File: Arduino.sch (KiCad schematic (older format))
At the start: 9 parts

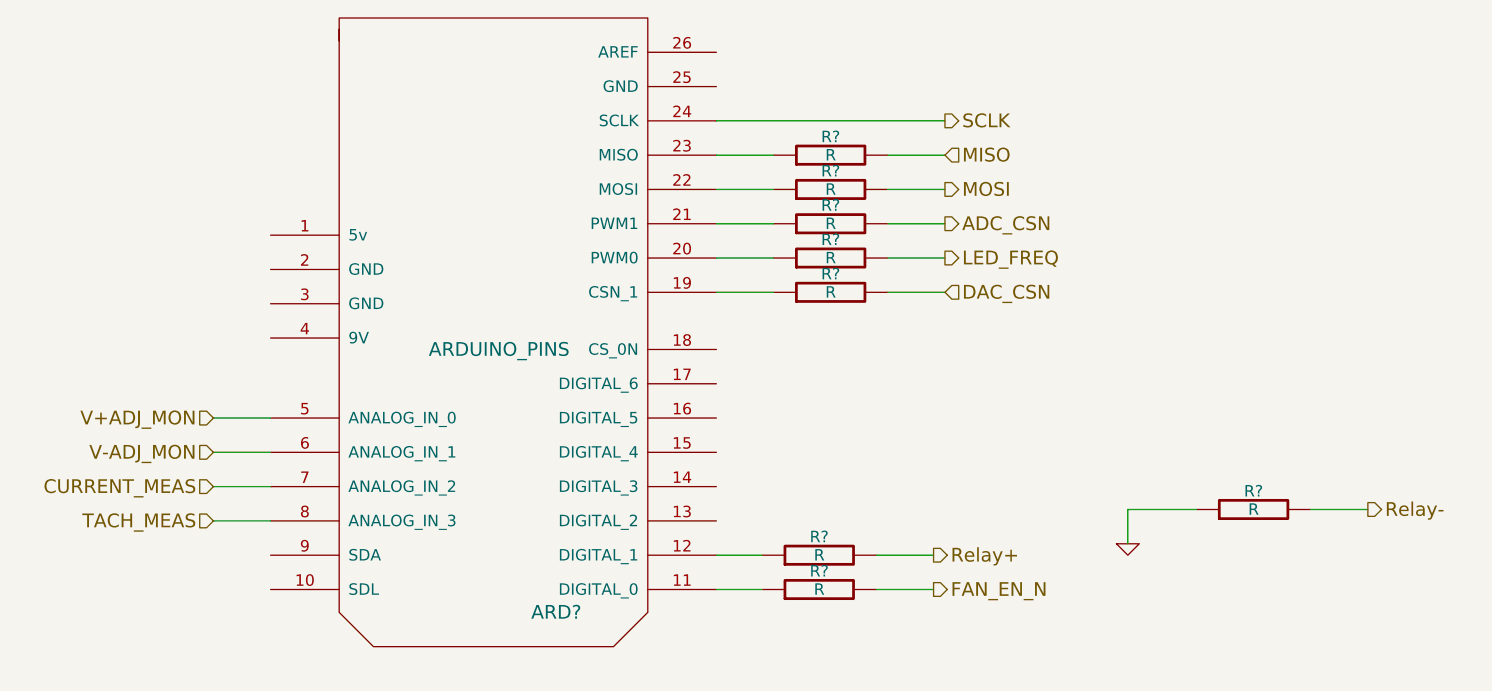
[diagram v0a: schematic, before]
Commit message: Fan/Current mode redo
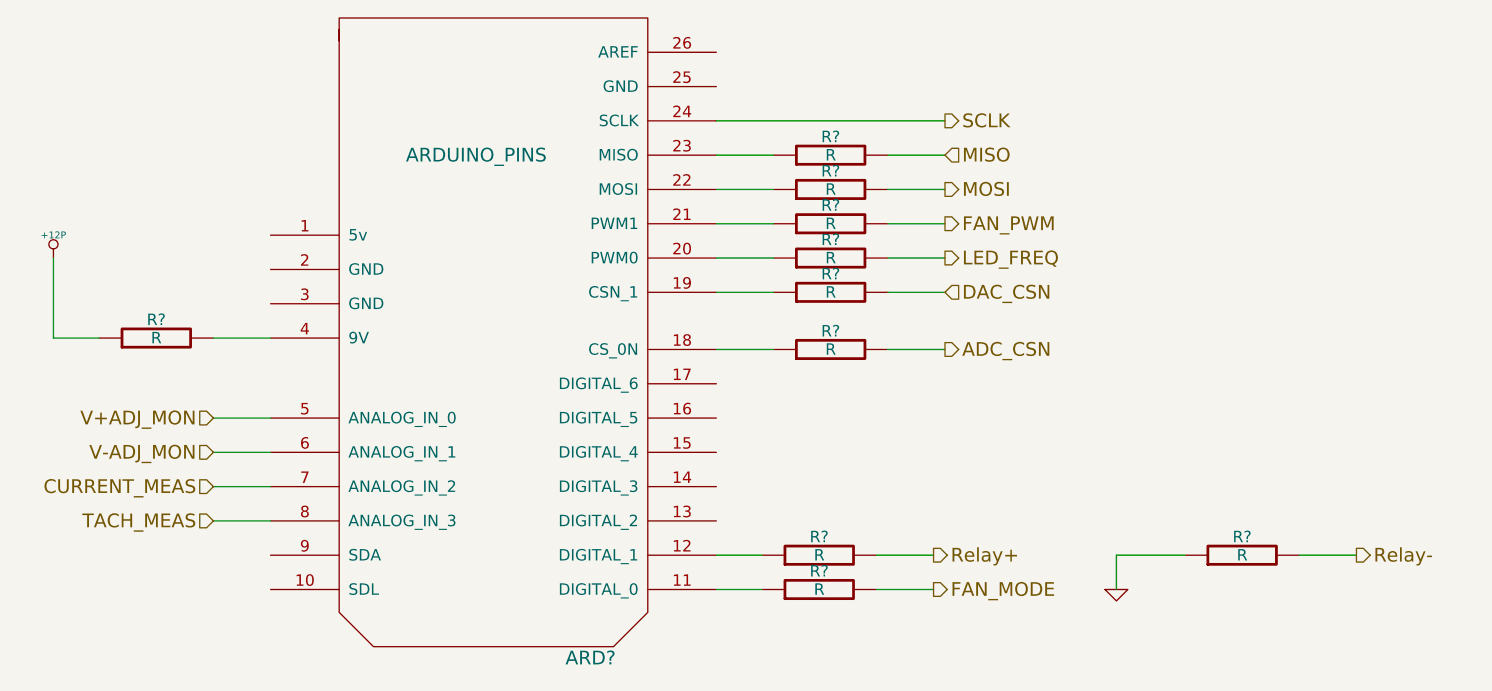
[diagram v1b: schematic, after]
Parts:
- removed ARD?: ARDUINO_PINS, symbol ARDUINO_PINS
- added ARD?: ARDUINO_PINS, symbol ARDUINO_PINS
- added R? (x2): R, symbol R
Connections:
- net ADC_CSN: now also R?.2; no longer R?.2
- net CURRENT_MEAS: now also ARD?.7 (ANALOG_IN_2)
- net SCLK: now also ARD?.24 (SCLK)
- net TACH_MEAS: now also ARD?.8 (ANALOG_IN_3)
- net V+ADJ_MON: now also ARD?.5 (ANALOG_IN_0)
- net V-ADJ_MON: now also ARD?.6 (ANALOG_IN_1)
- net at R?.1: now also ARD?.11 (DIGITAL_0)
- net at R?.1: now also ARD?.12 (DIGITAL_1)
- net at R?.1: now also ARD?.19 (CSN_1)
- net at R?.1: now also ARD?.20 (PWM0)
- net at R?.1: now also ARD?.21 (PWM1)
- net at R?.1: now also ARD?.22 (MOSI)
- net at R?.1: now also ARD?.23 (MISO)
- net FAN_EN_N renamed FAN_MODE
- new net: ARD?.18 (CS_0N), R?.1
- new net: ARD?.4 (9V), R?.2
- new net +12P: R?.1
- new net FAN_PWM: R?.2
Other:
- moved on the sheet: R?
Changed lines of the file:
@@
-EESchema Schematic File Version 2  date Sat 08 Feb 2014 11:37:49 PM EST
+EESchema Schematic File Version 2  date Sun 09 Feb 2014 12:22:09 AM EST
 LIBS:power
 LIBS:device
@@
 $EndDescr
 Wire Wire Line
+	4300 3950 4100 3950
+Wire Wire Line
+	4100 3950 4100 3600
+Wire Wire Line
+	7750 4000 8000 4000
+Wire Wire Line
 	8000 3750 7750 3750
 Wire Wire Line
-	9600 4700 9850 4700
+	9550 4900 9800 4900
 Wire Wire Line
 	7750 3450 8000 3450
@@
 	4800 4600 5050 4600
 Wire Wire Line
-	8800 4850 8800 4700
+	8750 5050 8750 4900
 Wire Wire Line
 	4800 4750 5050 4750
@@
 	7750 3300 8000 3300
 Wire Wire Line
-	8800 4700 9100 4700
+	8750 4900 9050 4900
 Wire Wire Line
 	7750 3600 8000 3600
+Wire Wire Line
+	7000 4000 7250 4000
+Wire Wire Line
+	4800 3950 5050 3950
+$Comp
+L +12P #PWR?
+U 1 1 52F71052
+P 4100 3600
+F 0 "#PWR?" H 4100 3570 30  0001 C CNN
+F 1 "+12P" H 4100 3700 30  0000 C CNN
+	1    4100 3600
+	1    0    0    -1
+$EndComp
+$Comp
+L R R?
+U 1 1 52F71047
+P 4550 3950
+F 0 "R?" V 4630 3950 50  0000 C CNN
+F 1 "R" V 4550 3950 50  0000 C CNN
+	1    4550 3950
+	0    -1   -1   0
+$EndComp
+$Comp
+L ARDUINO_PINS ARD?
+U 1 1 52F70E5D
+P 6050 3950
+F 0 "ARD?" H 6450 2550 60  0000 C CNN
+F 1 "ARDUINO_PINS" H 5950 4750 60  0000 C CNN
+	1    6050 3950
+	1    0    0    -1
+$EndComp
+$Comp
+L R R?
+U 1 1 52F70DB3
+P 7500 4000
+F 0 "R?" V 7580 4000 50  0000 C CNN
+F 1 "R" V 7500 4000 50  0000 C CNN
+	1    7500 4000
+	0    -1   -1   0
+$EndComp
+Text HLabel 8000 3450 2    60   Output ~ 0
+FAN_PWM
 Text HLabel 8000 3750 2    60   Input ~ 0
 DAC_CSN
@@
 L R R?
 U 1 1 52F700CE
-P 9350 4700
-F 0 "R?" V 9430 4700 50  0000 C CNN
-F 1 "R" V 9350 4700 50  0000 C CNN
-	1    9350 4700
+P 9300 4900
+F 0 "R?" V 9380 4900 50  0000 C CNN
+F 1 "R" V 9300 4900 50  0000 C CNN
+	1    9300 4900
 	0    -1   -1   0
 $EndComp
@@
 L GND #PWR?
 U 1 1 52F6FBAC
-P 8800 4850
-F 0 "#PWR?" H 8800 4850 30  0001 C CNN
-F 1 "GND" H 8800 4780 30  0001 C CNN
-	1    8800 4850
+P 8750 5050
+F 0 "#PWR?" H 8750 5050 30  0001 C CNN
+F 1 "GND" H 8750 4980 30  0001 C CNN
+	1    8750 5050
 	1    0    0    -1
 $EndComp
@@
 Text HLabel 4800 4600 0    60   Input ~ 0
 CURRENT_MEAS
-$Comp
-L ARDUINO_PINS ARD?
-U 1 1 52F6F8AD
-P 6050 3950
-F 0 "ARD?" H 6300 2750 60  0000 C CNN
-F 1 "ARDUINO_PINS" H 6050 3900 60  0000 C CNN
-	1    6050 3950
-	1    0    0    -1
-$EndComp
 Text HLabel 4800 4750 0    60   Input ~ 0
 TACH_MEAS
 Text HLabel 7950 5050 2    60   Output ~ 0
-FAN_EN_N
+FAN_MODE
 Text HLabel 8000 3600 2    60   Output ~ 0
 LED_FREQ
-Text HLabel 8000 3450 2    60   Output ~ 0
+Text HLabel 8000 4000 2    60   Output ~ 0
 ADC_CSN
 Text HLabel 8000 3000 2    60   Output ~ 0
@@
 Text HLabel 8000 3300 2    60   Output ~ 0
 MOSI
-Text HLabel 9850 4700 2    60   Output ~ 0
+Text HLabel 9800 4900 2    60   Output ~ 0
 Relay-
 Text HLabel 7950 4900 2    60   Output ~ 0
